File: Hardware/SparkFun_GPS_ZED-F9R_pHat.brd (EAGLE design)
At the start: 65 x 57.3 mm, 113 parts, among them J1 U.FL, J5 QWIIC_RIGHT_ANGLE, J6 RASPBERRYPI-40-PIN-GPIO_SMD_S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, U1 U-BLOX_ZED_F9R, U2 DUAL-OPTO_HCPL-073L, U3 UHS_INVERTER_SCHMITT_TRIGGERS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, U4 UHS_INVERTER_SCHMITT_TRIGGERS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

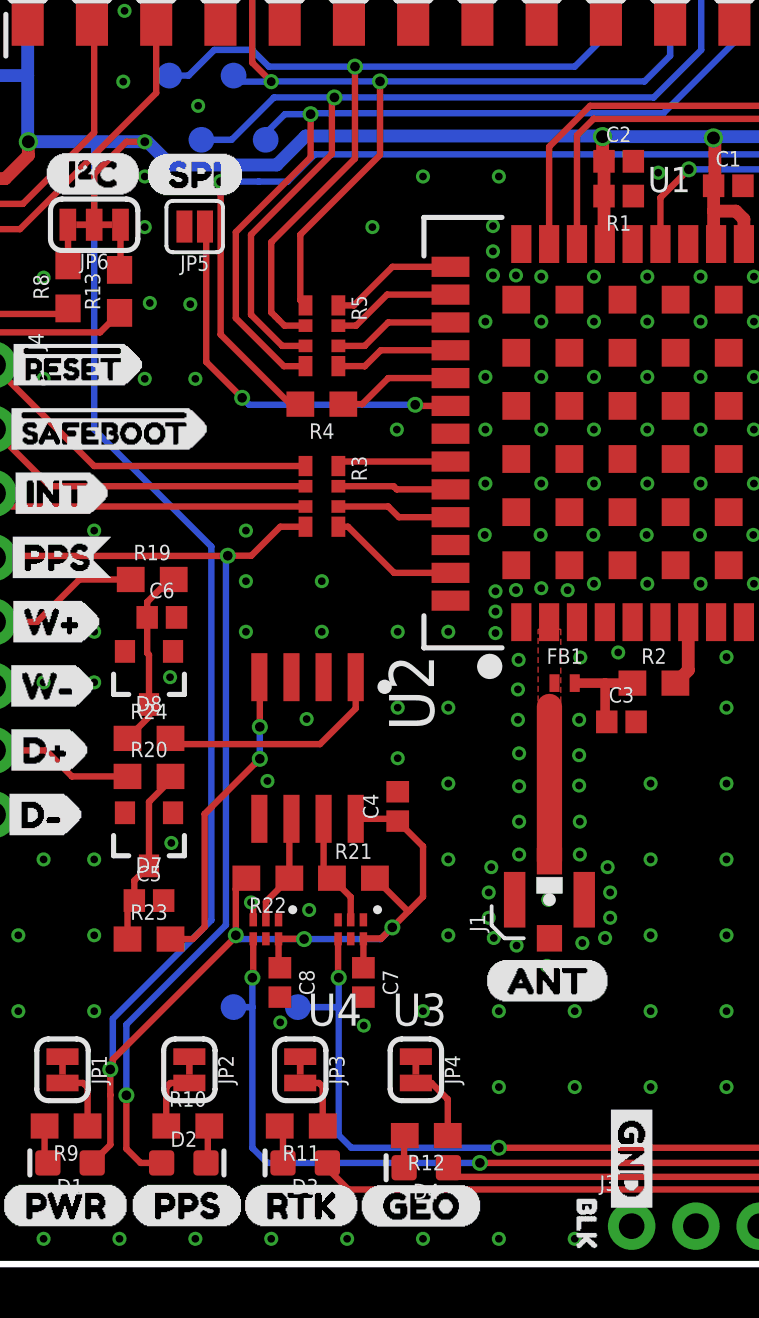
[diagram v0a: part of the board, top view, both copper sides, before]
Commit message: Fixes issue with panel
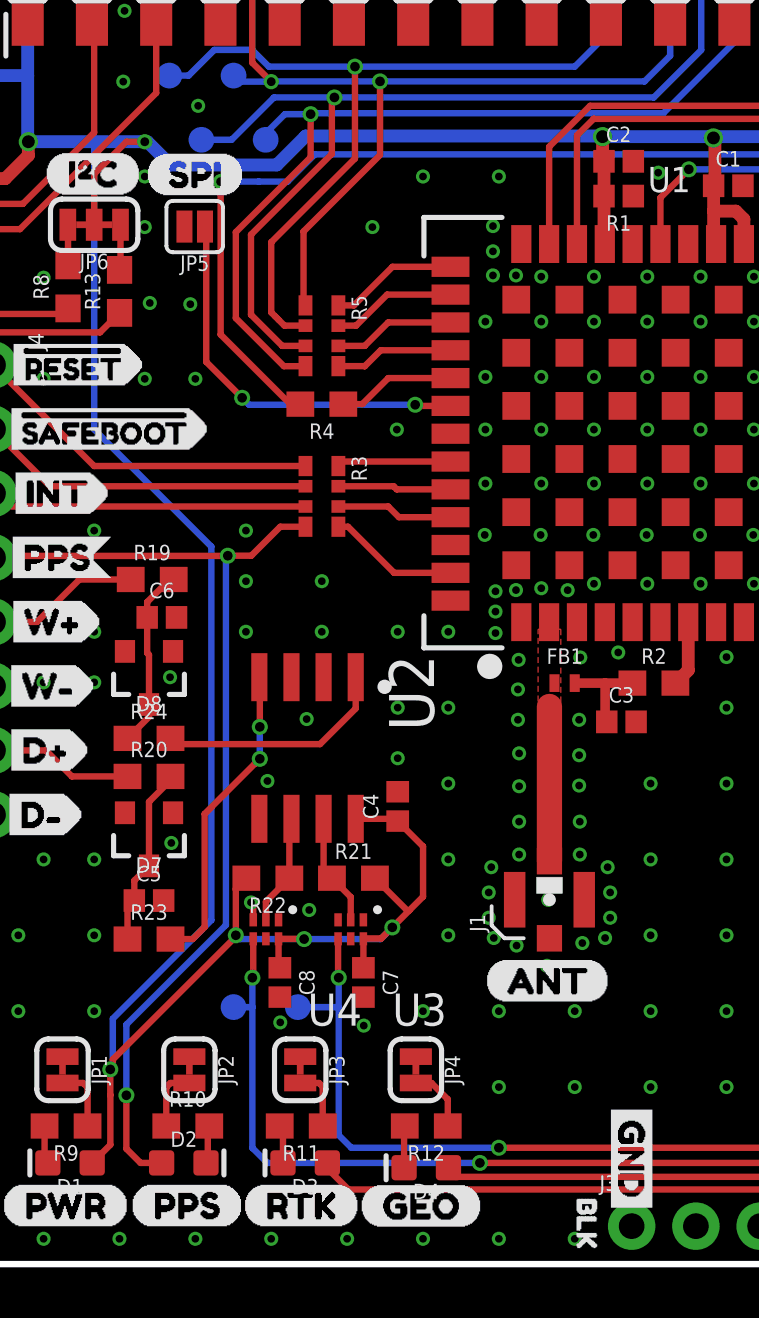
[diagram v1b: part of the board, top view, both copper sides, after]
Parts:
- moved R12 0.38 mm to (24.1, 5.46)
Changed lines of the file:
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@@
 <attribute name="VALUE" x="52.619" y="13.016" size="0.6096" layer="27" font="vector" ratio="20" rot="R90" align="top-center"/>
 </element>
-<element name="R12" library="SparkFun-Resistors" package="0603" value="1k" x="24.13" y="5.08" smashed="yes" rot="R180">
-<attribute name="NAME" x="24.13" y="4.318" size="0.6096" layer="25" font="vector" ratio="20" rot="R180" align="bottom-center"/>
-<attribute name="PROD_ID" value="RES-07856" x="24.13" y="0" size="1.778" layer="27" font="vector" ratio="15" rot="R180" display="off"/>
-<attribute name="VALUE" x="24.13" y="5.842" size="0.6096" layer="27" font="vector" ratio="20" rot="R180" align="top-center"/>
+<element name="R12" library="SparkFun-Resistors" package="0603" value="1k" x="24.13" y="5.461" smashed="yes" rot="R180">
+<attribute name="NAME" x="24.13" y="4.699" size="0.6096" layer="25" font="vector" ratio="20" rot="R180" align="bottom-center"/>
+<attribute name="PROD_ID" value="RES-07856" x="24.13" y="0.381" size="1.778" layer="27" font="vector" ratio="15" rot="R180" display="off"/>
+<attribute name="VALUE" x="24.13" y="6.223" size="0.6096" layer="27" font="vector" ratio="20" rot="R180" align="top-center"/>
 </element>
 <element name="JP4" library="SparkFun-Jumpers" package="SMT-JUMPER_2_NC_TRACE_SILK" package3d_urn="urn:adsk.eagle:package:39281/1" value="JUMPER-SMT_2_NC_TRACE_SILK" x="23.718" y="7.6815" smashed="yes" rot="R270">
@@
 <wire x1="18" y1="46.75" x2="17.25" y2="47.5" width="0.254" layer="1"/>
 <wire x1="17.25" y1="47.5" x2="17.25" y2="54.842" width="0.254" layer="1"/>
-<wire x1="19.15" y1="40.7" x2="22.3012" y2="43.8512" width="0.254" layer="1"/>
+<wire x1="19.277" y1="40.827" x2="22.3012" y2="43.8512" width="0.254" layer="1"/>
 <wire x1="22.3012" y1="43.8512" x2="22.3012" y2="46.76" width="0.254" layer="1"/>
 <contactref element="TP2" pad="P$1"/>
@@
 <wire x1="18.1795" y1="54.864" x2="17.272" y2="54.864" width="0.254" layer="1"/>
 <contactref element="R5" pad="P1"/>
-<wire x1="19.3546" y1="37.903" x2="19.15" y2="38.1076" width="0.254" layer="1"/>
-<wire x1="19.15" y1="38.1076" x2="19.15" y2="40.7" width="0.254" layer="1"/>
+<wire x1="19.3546" y1="37.903" x2="19.277" y2="37.9806" width="0.254" layer="1"/>
+<wire x1="19.277" y1="37.9806" x2="19.277" y2="40.827" width="0.254" layer="1"/>
 </signal>
 <signal name="D_SEL">
@@
 <contactref element="JP4" pad="2"/>
 <contactref element="R12" pad="1"/>
-<wire x1="24.98" y1="5.08" x2="24.98" y2="6.516" width="0.254" layer="1"/>
+<wire x1="24.98" y1="5.461" x2="24.98" y2="6.516" width="0.254" layer="1"/>
 <wire x1="24.3352" y1="7.1608" x2="23.718" y2="7.1608" width="0.254" layer="1"/>
 <wire x1="24.98" y1="6.516" x2="24.3352" y2="7.1608" width="0.254" layer="1"/>
@@
 <contactref element="R12" pad="2"/>
 <contactref element="D4" pad="C"/>
-<wire x1="23.253" y1="3.81" x2="23.253" y2="5.053" width="0.254" layer="1"/>
-<wire x1="23.253" y1="5.053" x2="23.28" y2="5.08" width="0.254" layer="1"/>
+<wire x1="23.253" y1="3.81" x2="23.253" y2="5.434" width="0.254" layer="1"/>
+<wire x1="23.253" y1="5.434" x2="23.28" y2="5.461" width="0.254" layer="1"/>
 </signal>
 <signal name="N$13">
